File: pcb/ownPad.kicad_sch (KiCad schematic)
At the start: 14 parts, among them J1 OLED_DISPLAY, SW1 RotaryEncoder_Switch, SW2 SW_Push, SW3 SW_Push, SW4 SW_Push, SW5 SW_Push, SW6 RotaryEncoder_Switch, U1 MOUDLE-SEEEDUINO-XIAO

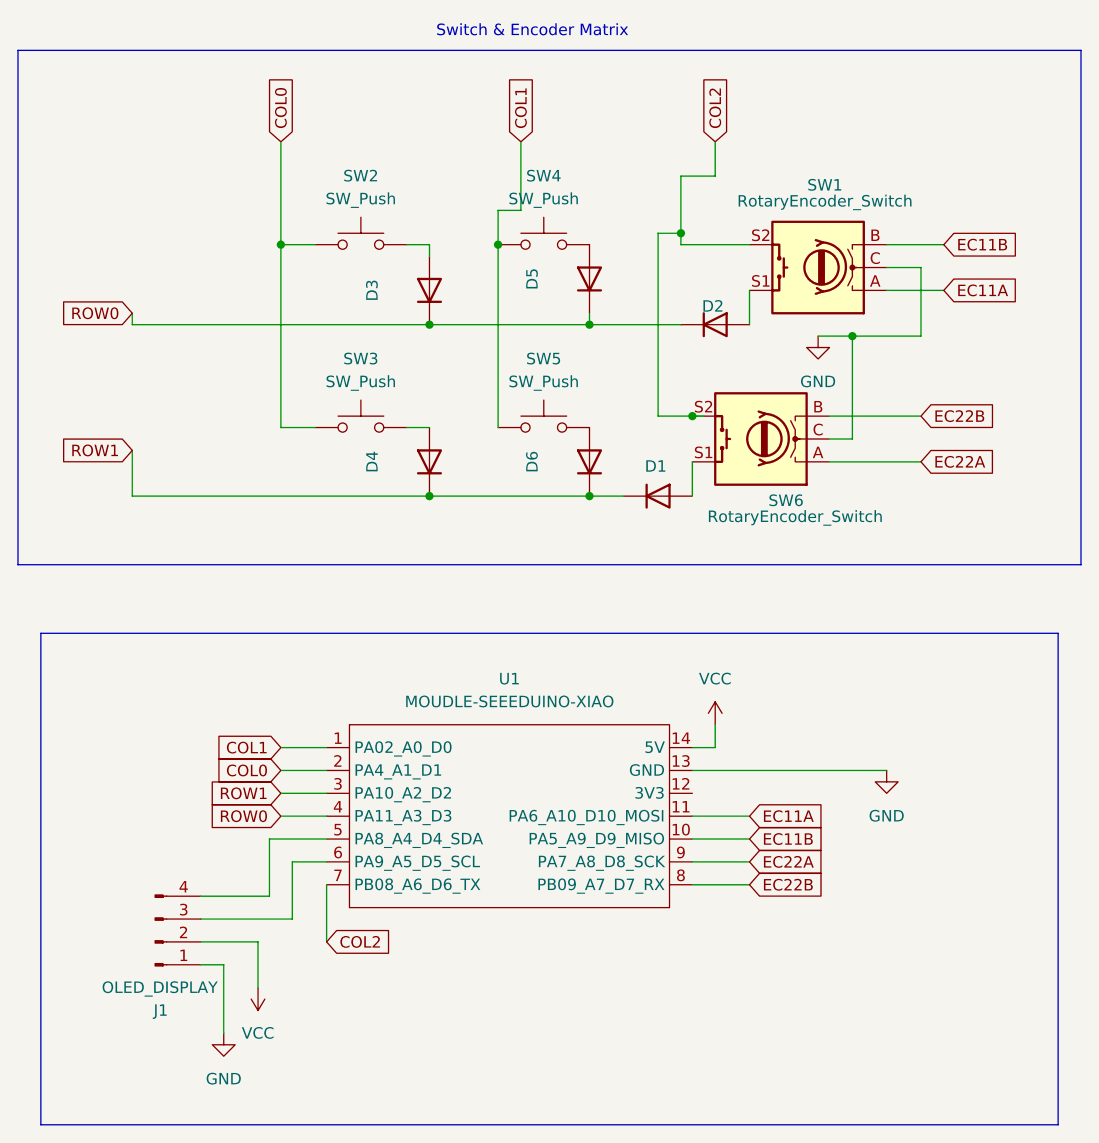
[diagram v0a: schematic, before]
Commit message: fixed unconnected traces on pcb
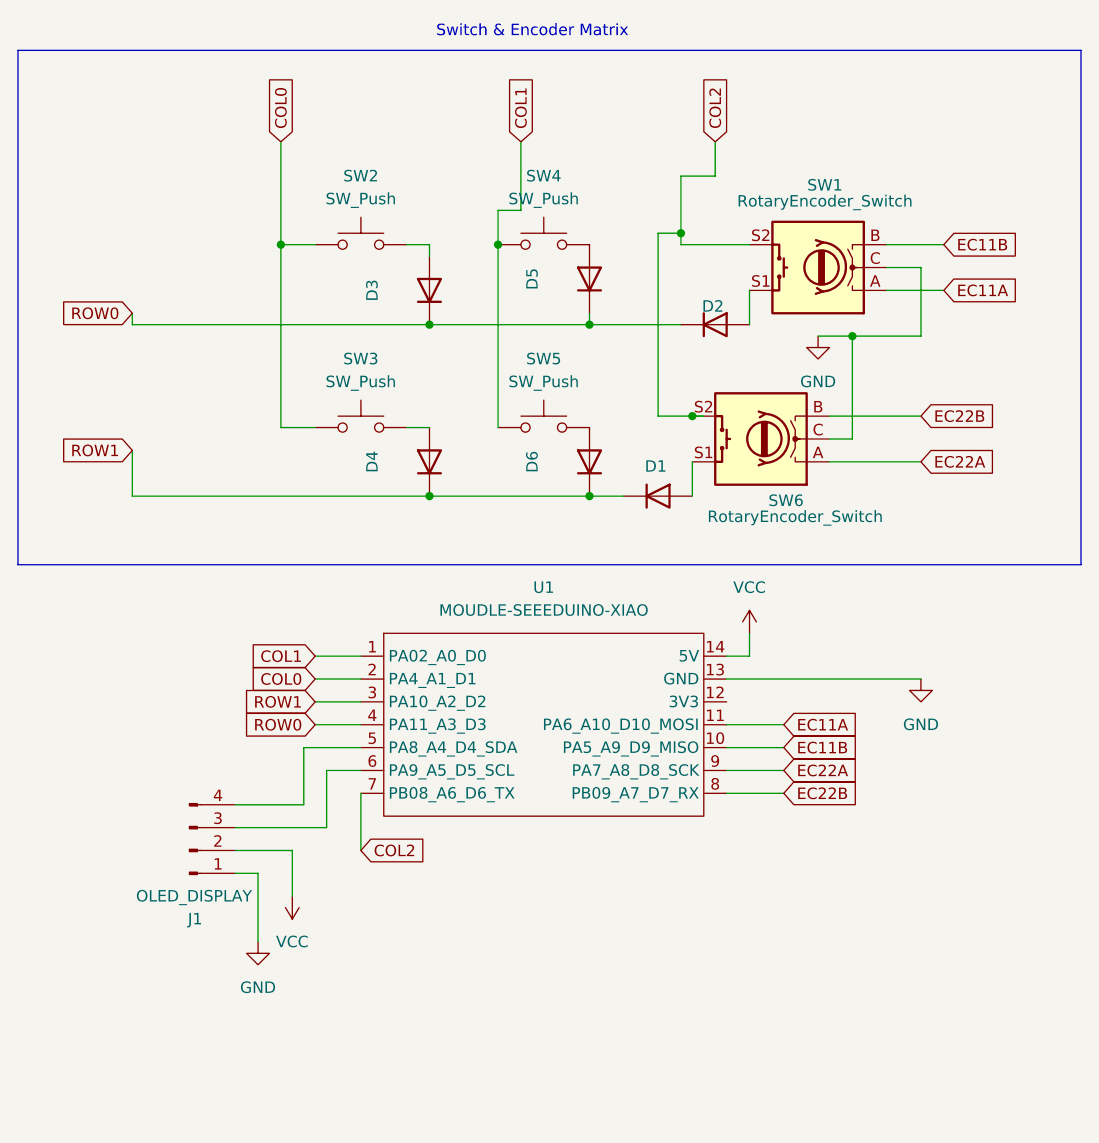
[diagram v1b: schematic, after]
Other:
- moved on the sheet: J1, U1

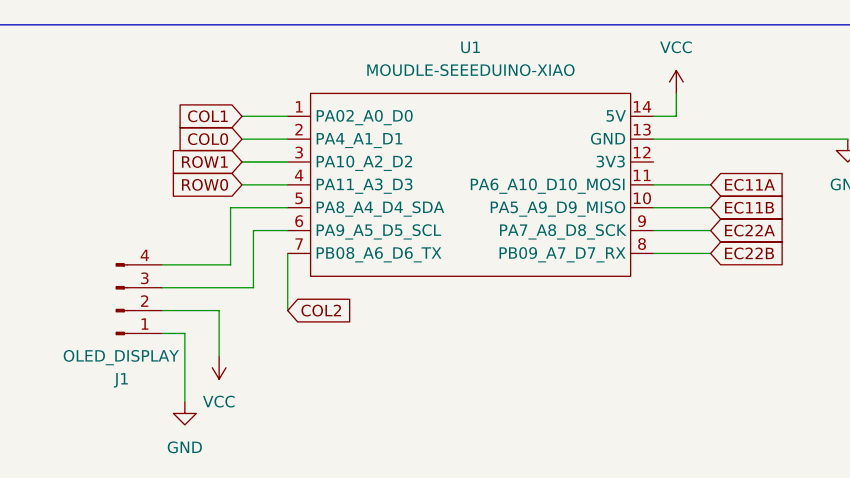
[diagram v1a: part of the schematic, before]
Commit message: removed errors in pcb design
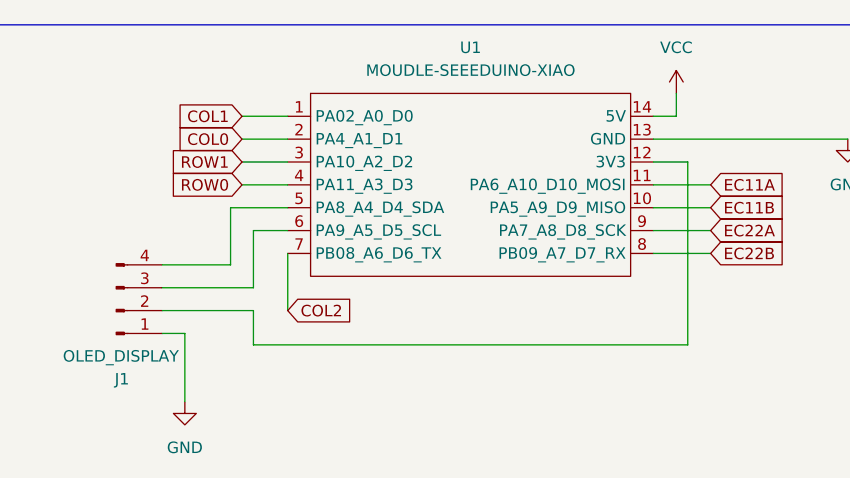
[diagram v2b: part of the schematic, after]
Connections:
- net VCC: no longer J1.2 (Pin_2)
- net at U1.12 (3V3): now also J1.2 (Pin_2)
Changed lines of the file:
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@@
+	(wire
+		(pts
+			(xy 92.71 90.17) (xy 96.52 90.17)
+		)
+		(stroke
+			(width 0)
+			(type default)
+		)
+	)
 	(wire
 		(pts
@@
 	(wire
 		(pts
-			(xy 44.45 106.68) (xy 44.45 111.76)
-		)
-		(stroke
-			(width 0)
-			(type default)
-		)
-	)
-	(wire
-		(pts
 			(xy 106.68 49.53) (xy 102.87 49.53)
 		)
@@
 	(wire
 		(pts
+			(xy 48.26 110.49) (xy 96.52 110.49)
+		)
+		(stroke
+			(width 0)
+			(type default)
+		)
+	)
+	(wire
+		(pts
 			(xy 92.71 87.63) (xy 114.3 87.63)
 		)
@@
 	(wire
 		(pts
-			(xy 38.1 106.68) (xy 44.45 106.68)
+			(xy 96.52 110.49) (xy 96.52 90.17)
+		)
+		(stroke
+			(width 0)
+			(type default)
+		)
+	)
+	(wire
+		(pts
+			(xy 48.26 106.68) (xy 48.26 110.49)
 		)
 		(stroke
@@
 		(pts
 			(xy 110.49 41.91) (xy 114.3 41.91)
+		)
+		(stroke
+			(width 0)
+			(type default)
+		)
+	)
+	(wire
+		(pts
+			(xy 38.1 106.68) (xy 48.26 106.68)
 		)
 		(stroke
@@
 					(unit 1)
 				)
-			)
-		)
-	)
-	(symbol
-		(lib_id "power:VCC")
-		(at 44.45 111.76 180)
-		(unit 1)
-		(exclude_from_sim no)
-		(in_bom yes)
-		(on_board yes)
-		(dnp no)
-		(fields_autoplaced yes)
-		(property "Reference" "#PWR02"
-			(at 44.45 107.95 0)
-			(effects
-				(font
-					(size 1.27 1.27)
-				)
-				(hide yes)
-			)
-		)
-		(property "Value" "VCC"
-			(at 44.45 116.84 0)
-			(effects
-				(font
-					(size 1.27 1.27)
-				)
-			)
-		)
-		(property "Footprint" ""
-			(at 44.45 111.76 0)
-			(effects
-				(font
-					(size 1.27 1.27)
-				)
-				(hide yes)
-			)
-		)
-		(property "Datasheet" ""
-			(at 44.45 111.76 0)
-			(effects
-				(font
-					(size 1.27 1.27)
-				)
-				(hide yes)
-			)
-		)
-		(property "Description" "Power symbol creates a global label with name \"VCC\""
-			(at 44.45 111.76 0)
-			(effects
-				(font
-					(size 1.27 1.27)
-				)
-				(hide yes)
-			)
-		)
-		(pin "1"
-		)
-		(instances
-			(project ""
-				(path "/914c1ed6-ec52-40a6-87b3-68251964bf7f"
-					(reference "#PWR02")
-					(unit 1)
-				)
